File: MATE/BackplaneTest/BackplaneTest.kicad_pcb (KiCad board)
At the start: 2 copper layers, 83.5 x 22 mm, 8 parts, among them J1 Power, J2 PCC, J3 ESCC, J4 CAN, U1 L7805CV

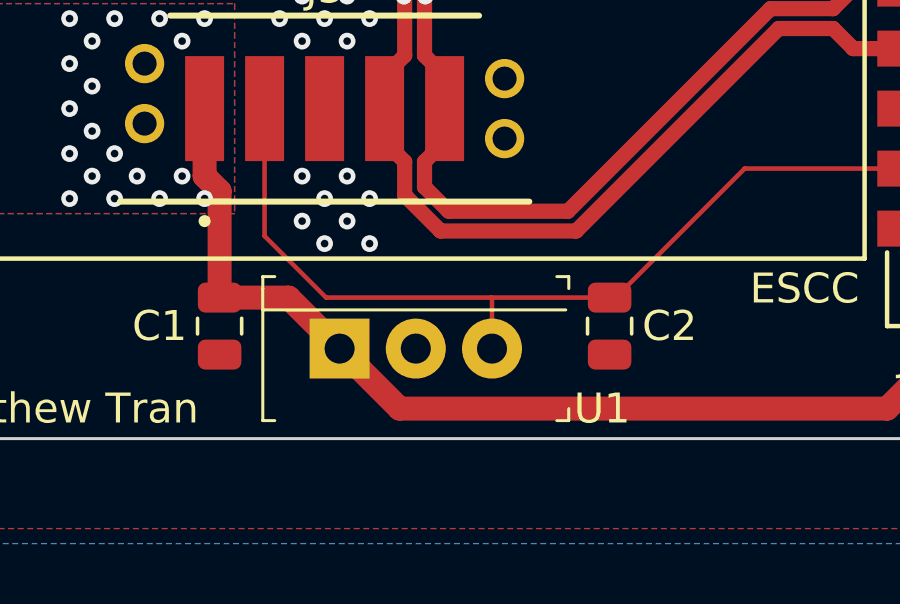
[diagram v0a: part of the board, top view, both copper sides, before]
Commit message: convert to kicad 6
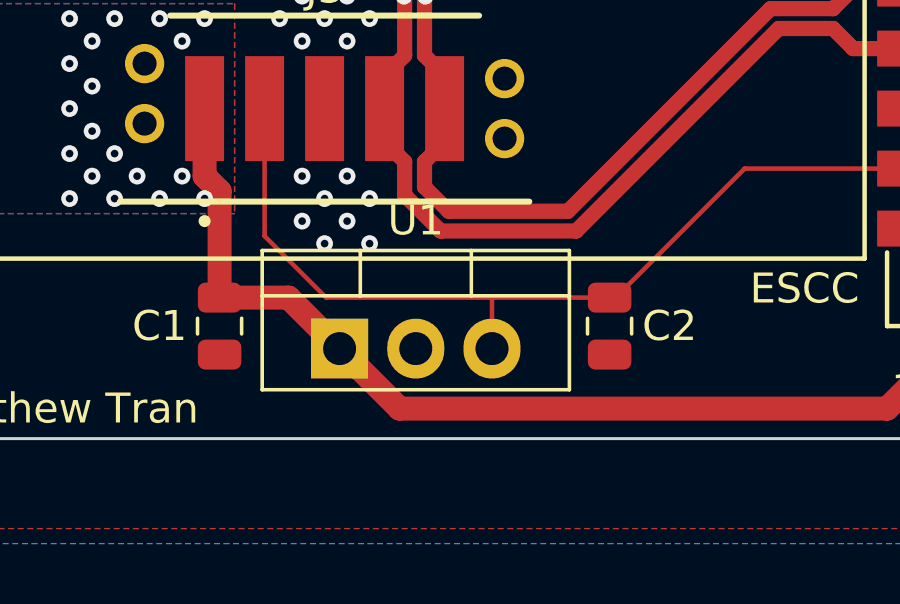
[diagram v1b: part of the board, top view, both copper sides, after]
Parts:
- U1: value L7805CV -> LM7805_TO220; footprint digikey-footprints:TO-220-3 -> Package_TO_SOT_THT:TO-220-3_Vertical
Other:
- net class Default removed
- net class Power removed
